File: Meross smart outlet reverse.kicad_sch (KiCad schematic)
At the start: 11 parts, among them SW1 SW_SPST

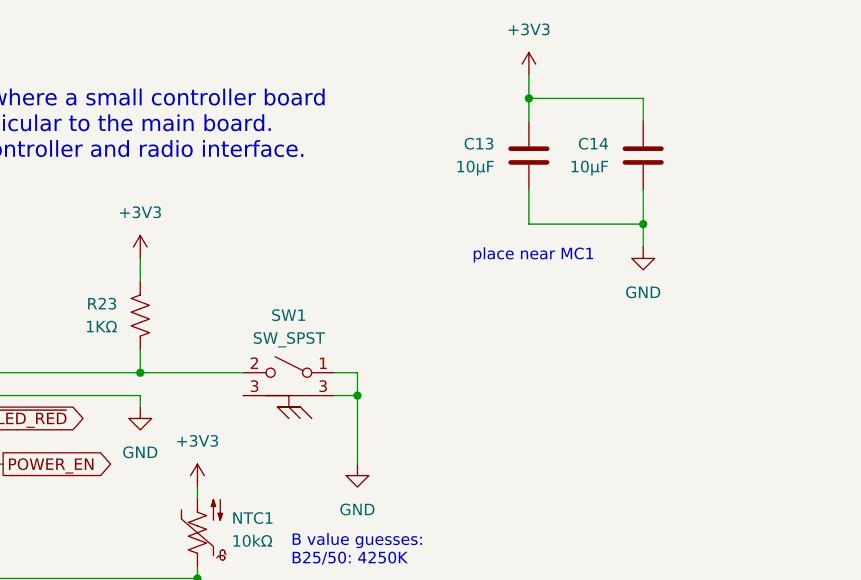
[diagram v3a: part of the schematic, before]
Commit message: Fixed silk, fixed fab. Fixed a few part 3D models. Starting to rename stuff.
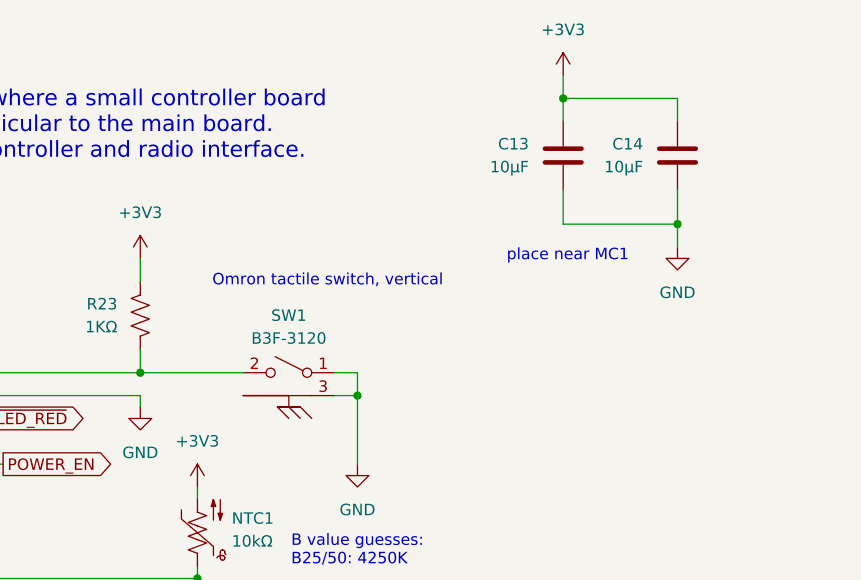
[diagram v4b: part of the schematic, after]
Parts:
- SW1: value SW_SPST -> B3F-3120
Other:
- note added: "Omron tactile switch, vertical"
- moved on the sheet: C13, C14
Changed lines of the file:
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@@
 	(title_block
 		(title "sensing and controlling interface")
-		(date "2025-07-25")
+		(date "2025-07-28")
 	)
 	(text "2.6"
@@
 		)
 	)
+	(text "Omron tactile switch, vertical"
+		(exclude_from_sim no)
+		(at 94.488 49.53 0)
+		(effects
+			(font
+				(size 1.27 1.27)
+			)
+		)
+	)
 	(text "3.0"
 		(exclude_from_sim no)
@@
 	(text "place near MC1"
 		(exclude_from_sim no)
-		(at 117.348 46.736 0)
+		(at 121.158 46.736 0)
 		(effects
 			(font
@@
 	)
 	(junction
-		(at 129.54 43.18)
+		(at 133.35 43.18)
 		(diameter 0)
 		(color 0 0 0 0)
@@
 	)
 	(junction
-		(at 116.84 29.21)
+		(at 120.65 29.21)
 		(diameter 0)
 		(color 0 0 0 0)
@@
 	(wire
 		(pts
-			(xy 116.84 29.21) (xy 129.54 29.21)
+			(xy 120.65 29.21) (xy 133.35 29.21)
 		)
 		(stroke
@@
 	(wire
 		(pts
-			(xy 116.84 26.67) (xy 116.84 29.21)
+			(xy 120.65 26.67) (xy 120.65 29.21)
 		)
 		(stroke
@@
 	(wire
 		(pts
-			(xy 129.54 29.21) (xy 129.54 31.75)
+			(xy 133.35 29.21) (xy 133.35 31.75)
 		)
 		(stroke
@@
 	(wire
 		(pts
-			(xy 129.54 39.37) (xy 129.54 43.18)
+			(xy 133.35 39.37) (xy 133.35 43.18)
 		)
 		(stroke
@@
 	(wire
 		(pts
-			(xy 116.84 29.21) (xy 116.84 31.75)
-		)
-		(stroke
-			(width 0)
-			(type default)
-		)
-	)
-	(wire
-		(pts
-			(xy 116.84 43.18) (xy 129.54 43.18)
+			(xy 120.65 29.21) (xy 120.65 31.75)
+		)
+		(stroke
+			(width 0)
+			(type default)
+		)
+	)
+	(wire
+		(pts
+			(xy 120.65 43.18) (xy 133.35 43.18)
 		)
 		(stroke
@@
 	(wire
 		(pts
-			(xy 116.84 39.37) (xy 116.84 43.18)
-		)
-		(stroke
-			(width 0)
-			(type default)
-		)
-	)
-	(wire
-		(pts
-			(xy 129.54 43.18) (xy 129.54 45.72)
+			(xy 120.65 39.37) (xy 120.65 43.18)
+		)
+		(stroke
+			(width 0)
+			(type default)
+		)
+	)
+	(wire
+		(pts
+			(xy 133.35 43.18) (xy 133.35 45.72)
 		)
 		(stroke
@@
 	(symbol
 		(lib_id "Device:C")
-		(at 129.54 35.56 0)
+		(at 133.35 35.56 0)
 		(mirror x)
 		(unit 1)
@@
 		(fields_autoplaced yes)
 		(property "Reference" "C14"
-			(at 125.73 34.2899 0)
+			(at 129.54 34.2899 0)
 			(effects
 				(font
@@
 		)
 		(property "Value" "10µF"
-			(at 125.73 36.8299 0)
+			(at 129.54 36.8299 0)
 			(effects
 				(font
@@
 		)
 		(property "Footprint" "Capacitor_SMD:C_0402_1005Metric"
-			(at 130.5052 31.75 0)
+			(at 134.3152 31.75 0)
 			(effects
 				(font
@@
 		)
 		(property "Datasheet" "~"
-			(at 129.54 35.56 0)
+			(at 133.35 35.56 0)
 			(effects
 				(font
@@
 		)
 		(property "Description" "Unpolarized capacitor"
-			(at 129.54 35.56 0)
+			(at 133.35 35.56 0)
 			(effects
 				(font
@@
 	(symbol
 		(lib_id "Device:C")
-		(at 116.84 35.56 0)
+		(at 120.65 35.56 0)
 		(mirror x)
 		(unit 1)
@@
 		(fields_autoplaced yes)
 		(property "Reference" "C13"
-			(at 113.03 34.2899 0)
+			(at 116.84 34.2899 0)
 			(effects
 				(font
@@
 		)
 		(property "Value" "10µF"
-			(at 113.03 36.8299 0)
+			(at 116.84 36.8299 0)
 			(effects
 				(font
@@
 		)
 		(property "Footprint" "Capacitor_SMD:C_0402_1005Metric"
-			(at 117.8052 31.75 0)
+			(at 121.6152 31.75 0)
 			(effects
 				(font
@@
 		)
 		(property "Datasheet" "~"
-			(at 116.84 35.56 0)
+			(at 120.65 35.56 0)
 			(effects
 				(font
@@
 		)
 		(property "Description" "Unpolarized capacitor"
-			(at 116.84 35.56 0)
+			(at 120.65 35.56 0)
 			(effects
 				(font
@@
 			)
 		)
-		(property "Value" "SW_SPST"
+		(property "Value" "B3F-3120"
 			(at 90.17 55.88 0)
 			(effects
@@
 		)
 		(pin "2"
-		)
-		(pin "3"
 		)
 		(pin "3"
@@
 	(symbol
 		(lib_id "power:GND")
-		(at 129.54 45.72 0)
+		(at 133.35 45.72 0)
 		(unit 1)
 		(exclude_from_sim no)
@@
 		(dnp no)
 		(property "Reference" "#PWR020"
-			(at 129.54 52.07 0)
+			(at 133.35 52.07 0)
 			(effects
 				(font
@@
 		)
 		(property "Value" "GND"
-			(at 129.54 50.8 0)
+			(at 133.35 50.8 0)
 			(effects
 				(font
@@
 		)
 		(property "Footprint" ""
-			(at 129.54 45.72 0)
+			(at 133.35 45.72 0)
 			(effects
 				(font
@@
 		)
 		(property "Datasheet" ""
-			(at 129.54 45.72 0)
+			(at 133.35 45.72 0)
 			(effects
 				(font
@@
 		)
 		(property "Description" "Power symbol creates a global label with name \"GND\" , ground"
-			(at 129.54 45.72 0)
+			(at 133.35 45.72 0)
 			(effects
 				(font
@@
 	(symbol
 		(lib_id "power:+3V3")
-		(at 116.84 26.67 0)
+		(at 120.65 26.67 0)
 		(mirror y)
 		(unit 1)
@@
 		(dnp no)
 		(property "Reference" "#PWR015"
-			(at 116.84 30.48 0)
+			(at 120.65 30.48 0)
 			(effects
 				(font
@@
 		)
 		(property "Value" "+3V3"
-			(at 116.84 21.59 0)
+			(at 120.65 21.59 0)
 			(effects
 				(font
@@
 		)
 		(property "Footprint" ""
-			(at 116.84 26.67 0)
+			(at 120.65 26.67 0)
 			(effects
 				(font
@@
 		)
 		(property "Datasheet" ""
-			(at 116.84 26.67 0)
+			(at 120.65 26.67 0)
 			(effects
 				(font
@@
 		)
 		(property "Description" "Power symbol creates a global label with name \"+3V3\""
-			(at 116.84 26.67 0)
-			(effects
-				(font
+			(at 120.65 26.67 0)
+			(effects
+				(font
